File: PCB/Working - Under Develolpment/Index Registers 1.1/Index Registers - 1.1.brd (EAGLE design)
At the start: 177.8 x 114.6 mm, 83 parts, among them IC1 74LS32N, IC10 74LS32N, IC11 74LS192N, IC12 74LS192N, IC13 74LS192N, IC14 74LS192N, IC15 74LS244N, IC16 74LS244N, IC17 74LS32N, IC18 74LS192N, IC19 74LS192N, IC2 74LS32N, IC20 74LS192N, IC21 74LS192N, IC22 74LS244N, IC23 74LS244N, IC24 74LS32N, IC25 74LS192N, IC26 74LS192N, IC27 74LS192N, IC28 74LS192N, IC29 74LS244N, IC3 74LS192N, IC30 74LS244N, IC31 74LS32N, IC32 74LS139N, IC33 74LS139N, IC34 4077N, IC35 74LS245N, IC36 74LS245N, IC37 74LS245N, IC4 74LS192N, IC5 74LS192N, IC6 74LS192N, IC7 74LS244N, IC8 74LS244N, IC9 74LS32N, X1 FABC96R

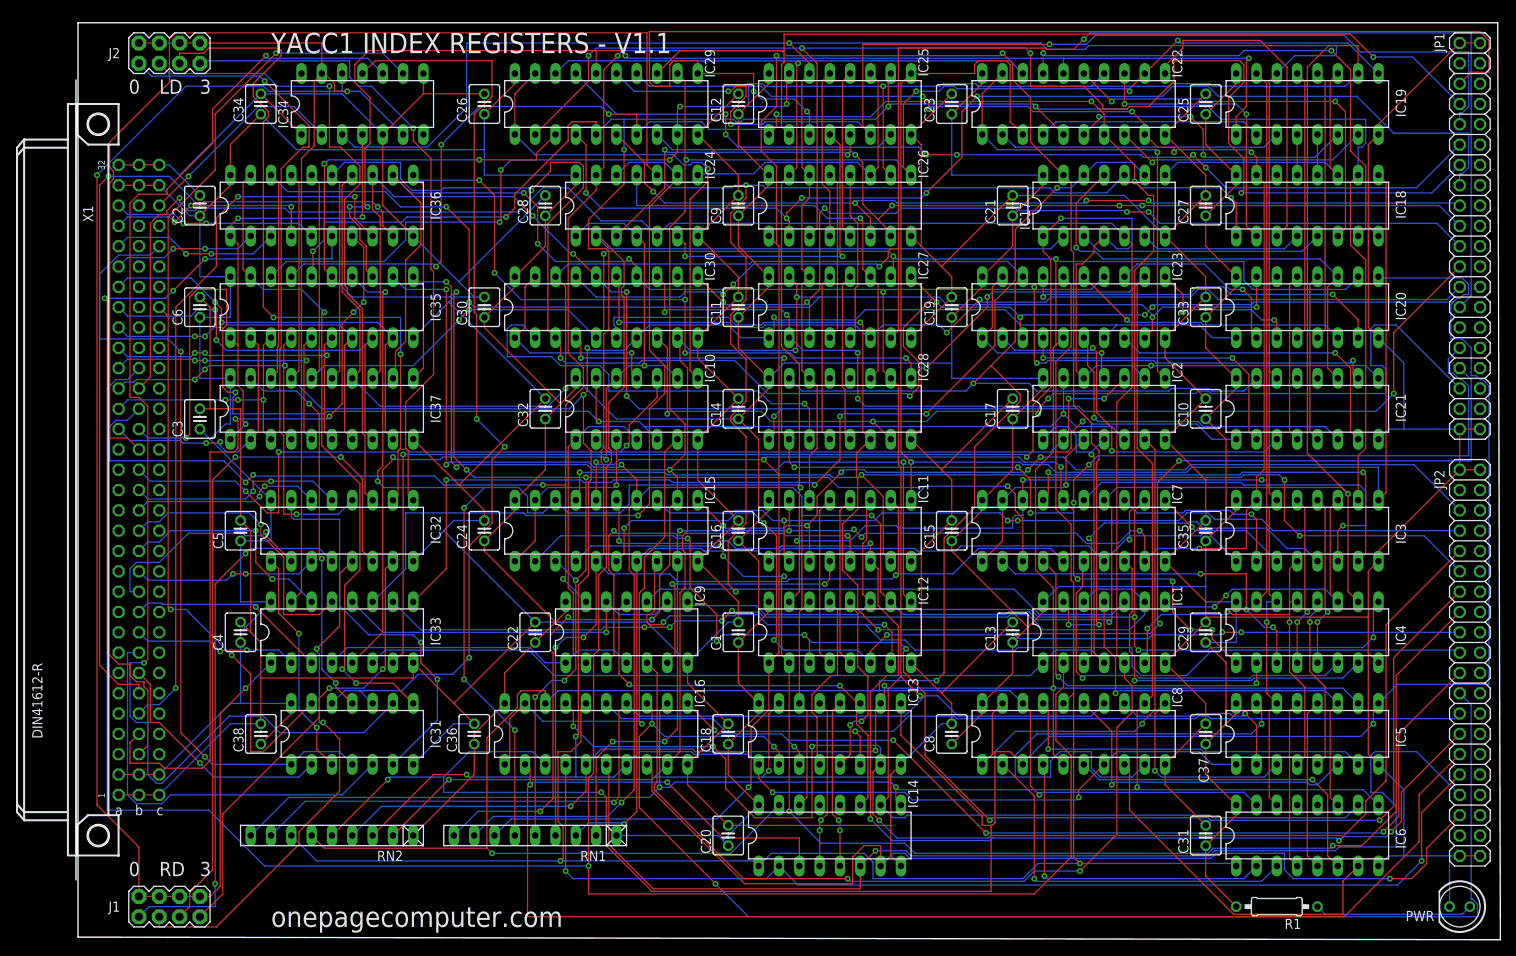
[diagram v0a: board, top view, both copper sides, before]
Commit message: Index Register Board V1.1
Modify so any data register can drive address bus
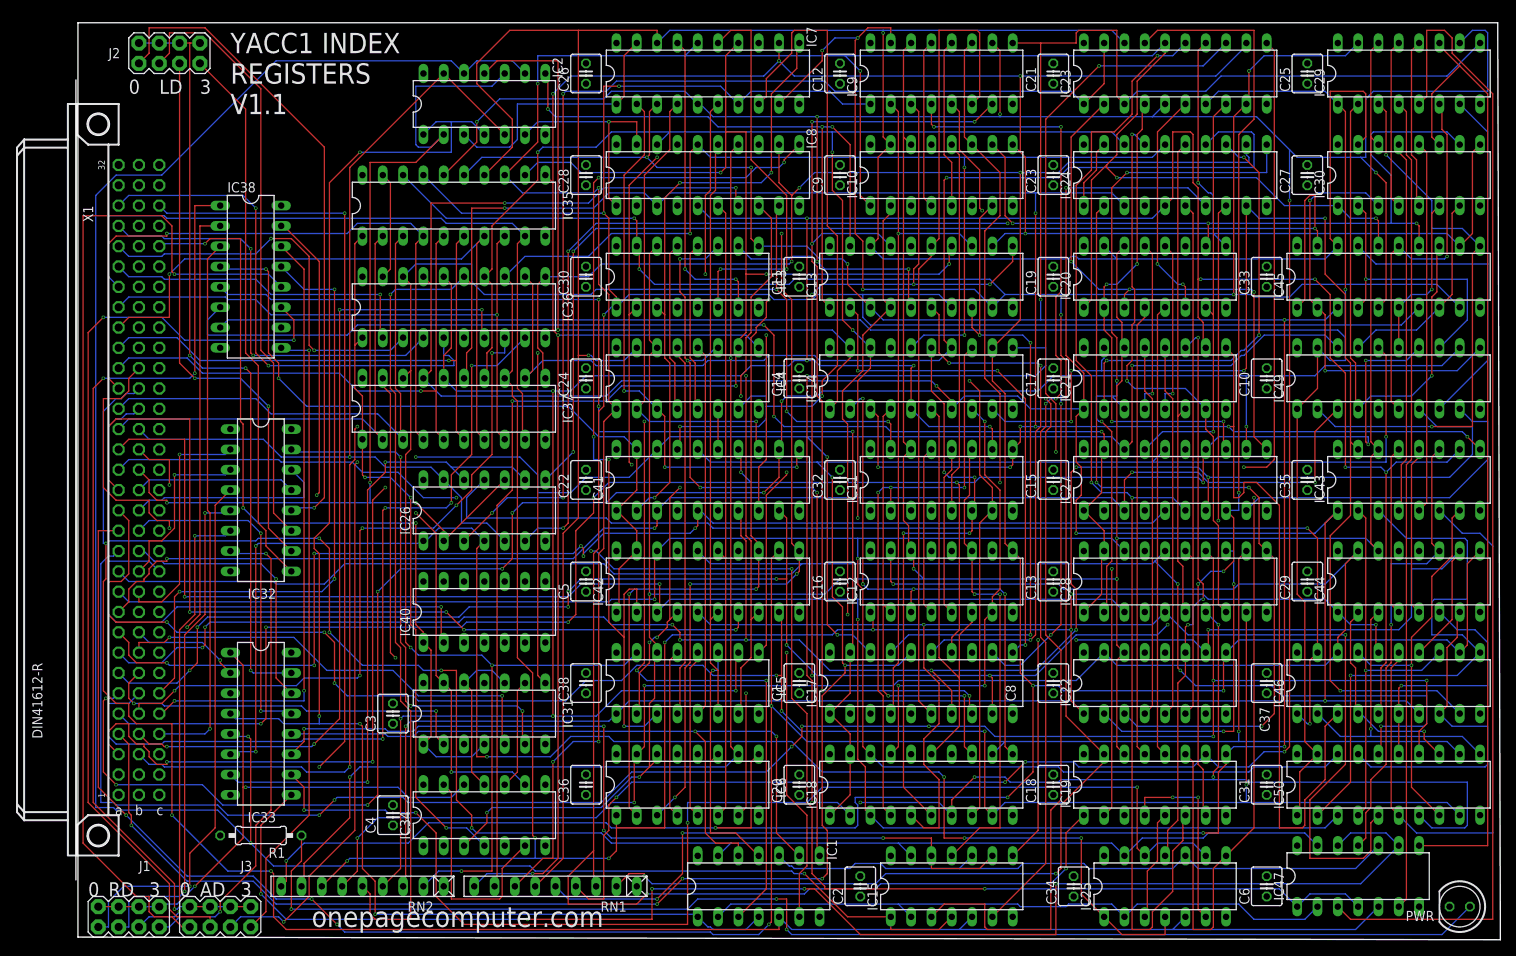
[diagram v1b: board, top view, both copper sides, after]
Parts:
- removed IC16: 74LS244N, 74xx-us:DIL20
- removed JP1, JP2: (no value), pinhead:2X20
- added IC38: 74LS139N, 74xx-us:DIL16
- added IC40, IC47: 74LS32N, 74xx-us:DIL14
- added IC41, IC42, IC45, IC46, IC49, IC50: 74LS244N, 74xx-us:DIL20
- added IC43, IC44: 74LS192N, 74xx-us:DIL16
- added J3: (no value), SparkFun-Connectors:2X4
- IC10, IC9: value 74LS32N -> 74LS192N; device 74xx-us:DIL14 -> 74xx-us:DIL16
- IC13, IC14, IC18, IC27, IC28: value 74LS192N -> 74LS244N; device 74xx-us:DIL16 -> 74xx-us:DIL20
- IC15: value 74LS244N -> 74LS32N; device 74xx-us:DIL20 -> 74xx-us:DIL14
- IC17, IC24: value 74LS32N -> 74LS244N; device 74xx-us:DIL14 -> 74xx-us:DIL20
- IC22, IC29, IC30: value 74LS244N -> 74LS192N; device 74xx-us:DIL20 -> 74xx-us:DIL16
- IC25, IC26: value 74LS192N -> 74LS32N; device 74xx-us:DIL16 -> 74xx-us:DIL14
- moved C6 151.7 mm to (148.6, 6.35)
- moved C34 141.0 mm to (124.5, 6.35)
- moved R1 127.3 mm to (22.9, 12.7)
- moved C2 118.6 mm to (97.8, 6.35)
- moved IC25 105.9 mm to (135.9, 6.35)
- moved IC30 101.7 mm to (166.4, 95.2)
- moved IC29 100.4 mm to (166.4, 108.0)
- moved IC34 90.2 mm to (50.8, 15.2)
- moved IC19 87.2 mm to (134.6, 19.1)
- moved IC18 87.0 mm to (105.4, 19.1)
- moved IC2 86.3 mm to (50.8, 104.1)
- moved IC3 83.7 mm to (76.2, 82.5)
- moved IC4 83.7 mm to (76.2, 69.8)
- moved IC8 83.5 mm to (78.7, 95.2)
- moved IC9 80.2 mm to (108.0, 108.0)
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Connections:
- net IO-ADDR0 renamed IOADDR0
- net IO-ADDR1 renamed IOADDR1
- net IO-ADDR2 renamed IOADDR2
- net IO-ADDR3 renamed IOADDR3
- removed net -ADDR-REG-LD0: X1.C4
- removed net -ADDR-REG-LD1: X1.C6
- removed net -ADDR-REG-RD0: X1.C3
- removed net -ADDR-REG-RD1: X1.C5
- removed net 1C-12: JP1.29
- removed net IA-0: IC11.3, IC15.11, JP2.5
- removed net IA-1: IC11.2, IC15.13, JP2.7
- removed net IA-10: IC13.6, IC16.15, JP2.25
- removed net IA-11: IC13.7, IC16.17, JP2.27
- removed net IA-12: IC14.3, IC16.2, JP2.29
- removed net IA-13: IC14.2, IC16.4, JP2.31
- removed net IA-14: IC14.6, IC16.6, JP2.33
- removed net IA-15: IC14.7, IC16.8, JP2.35
- removed net IA-2: IC11.6, IC15.15, JP2.9
- removed net IA-3: IC11.7, IC15.17, JP2.11
- removed net IA-4: IC12.3, IC15.2, JP2.13
- removed net IA-5: IC12.2, IC15.4, JP2.15
- removed net IA-6: IC12.6, IC15.6, JP2.17
- removed net IA-7: IC12.7, IC15.8, JP2.19
- removed net IA-8: IC13.3, IC16.11, JP2.21
- removed net IA-9: IC13.2, IC16.13, JP2.23
- removed net IB-0: JP2.6
- removed net IB-1: JP2.8
- removed net IB-10: JP2.26
- removed net IB-11: JP2.28
- removed net IB-12: JP2.30
- removed net IB-13: JP2.32
- removed net IB-14: JP2.34
- removed net IB-15: JP2.36
- removed net IB-2: JP2.10
- removed net IB-3: JP2.12
- removed net IB-4: JP2.14
- removed net IB-5: JP2.16
- removed net IB-6: JP2.18
- removed net IB-7: JP2.20
- removed net IB-8: JP2.22
- removed net IB-9: JP2.24
- removed net IC-0: IC25.3, IC29.11, JP1.5
- removed net IC-1: IC25.2, IC29.13, JP1.7
- removed net IC-10: IC27.6, IC30.15, JP1.25
- removed net IC-11: IC27.7, IC30.17, JP1.27
- removed net IC-12: IC28.3, IC30.2
- removed net IC-13: IC28.2, IC30.4, JP1.31
- removed net IC-14: IC28.6, IC30.6, JP1.33
- removed net IC-15: IC28.7, IC30.8, JP1.35
- removed net IC-2: IC25.6, IC29.15, JP1.9
- removed net IC-3: IC25.7, IC29.17, JP1.11
- removed net IC-4: IC26.3, IC29.2, JP1.13
- removed net IC-5: IC26.2, IC29.4, JP1.15
- removed net IC-6: IC26.6, IC29.6, JP1.17
- removed net IC-7: IC26.7, IC29.8, JP1.19
- removed net IC-8: IC27.3, IC30.11, JP1.21
- removed net IC-9: IC27.2, IC30.13, JP1.23
- removed net ID-0: JP1.6
- removed net ID-1: JP1.8
- removed net ID-10: JP1.26
- removed net ID-11: JP1.28
- removed net ID-12: JP1.30
- removed net ID-13: JP1.32
- removed net ID-14: JP1.34
- removed net ID-15: JP1.36
- removed net ID-2: JP1.10
- removed net ID-3: JP1.12
- removed net ID-4: JP1.14
- removed net ID-5: JP1.16
- removed net ID-6: JP1.18
- removed net ID-7: JP1.20
- removed net ID-8: JP1.22
- removed net ID-9: JP1.24
- removed net N$58 (its old number): IC18.13, IC19.4
- removed net N$59 (its old number): IC18.12, IC19.5
- removed net N$6 (its old number): IC27.13, IC28.4
- removed net N$7 (its old number): IC27.12, IC28.5
- removed net UNUSED0: X1.C12
- new net -ADDRSEL: IC38.1, J3.2, J3.4, J3.6, J3.8
- new net -ARD0: IC38.12, J3.1
- new net -R0-ADDRSEL: IC38.4, IC41.1, IC41.19, IC42.1, IC42.19
- new net -R1-ADDRSEL: IC17.1, IC17.19, IC18.1, IC18.19, IC38.5
- new net -R2-ADDRSEL: IC27.1, IC27.19, IC28.1, IC28.19, IC38.6
- new net -R3-ADDRSEL: IC38.7, IC49.1, IC49.19, IC50.1, IC50.19
- new net -VMA: IC40.2, X1.C12
- new net ADDR-REG-ID0: IC38.2, X1.C3
- new net ADDR-REG-ID1: IC38.3, X1.C4
- new net ADDR-REG-ID2: IC38.14, X1.C5
- new net ADDR-REG-ID3: IC38.13, X1.C6
- new net N$100: IC29.6, IC45.15, IC49.6
- new net N$101: IC29.7, IC45.17, IC49.8
- new net N$102: IC30.3, IC45.2, IC49.11
- new net N$103: IC30.2, IC45.4, IC49.13
- new net N$104: IC30.6, IC45.6, IC49.15
- new net N$105: IC30.7, IC45.8, IC49.17
- new net N$106: IC43.3, IC46.11, IC50.2
- new net N$107: IC43.2, IC46.13, IC50.4
- new net N$108: IC43.6, IC46.15, IC50.6
- new net N$109: IC43.7, IC46.17, IC50.8
- new net N$110: IC44.3, IC46.2, IC50.11
- new net N$111: IC44.2, IC46.4, IC50.13
- new net N$112: IC44.6, IC46.6, IC50.15
- new net N$113: IC44.7, IC46.8, IC50.17
- new net N$28: IC13.11, IC17.2, IC9.3
- new net N$29: IC13.13, IC17.4, IC9.2
- new net N$45: IC38.15, IC40.3
- new net N$51: IC38.11, J3.3
- new net N$52: IC38.10, J3.5
- new net N$53: IC38.9, J3.7
- new net N$54: IC12.3, IC14.2, IC18.11
- new net N$55: IC12.2, IC14.4, IC18.13
- new net N$56: IC12.6, IC14.6, IC18.15
- new net N$57: IC12.7, IC14.8, IC18.17
- new net N$62: IC21.13, IC22.4
- new net N$63: IC21.12, IC22.5
- new net N$67: IC23.1, IC23.19, IC26.3
- new net N$68: IC24.1, IC24.19, IC26.6
- new net N$69: IC21.11, IC22.11, IC25.11
- new net N$70: IC19.3, IC23.11, IC27.2
- new net N$71: IC19.2, IC23.13, IC27.4
- new net N$72: IC19.6, IC23.15, IC27.6
- new net N$73: IC19.7, IC23.17, IC27.8
- new net N$74: IC20.3, IC23.2, IC27.11
- new net N$75: IC20.2, IC23.4, IC27.13
- new net N$76: IC20.6, IC23.6, IC27.15
- new net N$77: IC20.7, IC23.8, IC27.17
- new net N$78: IC21.3, IC24.11, IC28.2
- new net N$79: IC21.2, IC24.13, IC28.4
- new net N$99: IC29.2, IC45.13, IC49.4
- net -BUS-EN: now also IC40.1
- net -R0-LDSEL: now also IC1.12, IC1.9; no longer IC9.12, IC9.9
- net -R0-RDSEL: now also IC1.1, IC1.4, IC2.1, IC2.4; no longer IC10.1, IC10.4, IC9.1, IC9.4
- net -R1-LDSEL: now also IC15.12, IC15.9; no longer IC24.12, IC24.9
- net -R1-RDSEL: now also IC15.1, IC15.4, IC2.12, IC2.9; no longer IC10.12, IC10.9, IC24.1, IC24.4
- net -R2-LDSEL: now also IC25.12, IC25.9; no longer IC1.12, IC1.9
- net -R2-RDSEL: now also IC25.1, IC25.4, IC26.1, IC26.4; no longer IC1.1, IC1.4, IC2.1, IC2.4
- net -R3-LDSEL: now also IC47.12, IC47.9; no longer IC17.12, IC17.9
- net -R3-RDSEL: now also IC26.12, IC26.9, IC47.1, IC47.4; no longer IC17.1, IC17.4, IC2.12, IC2.9
- net -REG-DN: now also IC15.5, IC25.5, IC47.5; no longer IC17.5, IC24.5, IC9.5
- net -REG-LD-HI: now also IC15.13, IC25.13, IC47.13; no longer IC17.13, IC24.13, IC9.13
- net -REG-LD-LO: now also IC15.10, IC25.10, IC47.10; no longer IC17.10, IC24.10, IC9.10
- net -REG-RD-HI: now also IC26.13, IC26.5; no longer IC10.13, IC10.5
- net -REG-RD-LO: now also IC26.10, IC26.2; no longer IC10.10, IC10.2
- net -REG-UP: now also IC15.2, IC25.2, IC47.2; no longer IC17.2, IC24.2, IC9.2
- net ADATA0: now also IC13.9, IC19.15, IC23.9, IC29.15, IC45.9, IC9.15; no longer IC11.15, IC15.9, IC18.15, IC22.9, IC25.15, IC29.9
- net ADATA1: now also IC13.7, IC19.1, IC23.7, IC29.1, IC45.7, IC9.1; no longer IC11.1, IC15.7, IC18.1, IC22.7, IC25.1, IC29.7
- net ADATA10: now also IC11.10, IC14.5, IC21.10, IC24.5, IC43.10, IC46.5; no longer IC13.10, IC16.5, IC20.10, IC23.5, IC27.10, IC30.5
- net ADATA11: now also IC11.9, IC14.3, IC21.9, IC24.3, IC43.9, IC46.3; no longer IC13.9, IC16.3, IC20.9, IC23.3, IC27.9, IC30.3
- net ADATA12: now also IC12.15, IC14.18, IC22.15, IC24.18, IC44.15, IC46.18; no longer IC14.15, IC16.18, IC21.15, IC23.18, IC28.15, IC30.18
- net ADATA13: now also IC12.1, IC14.16, IC22.1, IC24.16, IC44.1, IC46.16; no longer IC14.1, IC16.16, IC21.1, IC23.16, IC28.1, IC30.16
- net ADATA14: now also IC12.10, IC14.14, IC22.10, IC24.14, IC44.10, IC46.14; no longer IC14.10, IC16.14, IC21.10, IC23.14, IC28.10, IC30.14
- net ADATA15: now also IC12.9, IC14.12, IC22.9, IC24.12, IC44.9, IC46.12; no longer IC14.9, IC16.12, IC21.9, IC23.12, IC28.9, IC30.12
- net ADATA2: now also IC13.5, IC19.10, IC23.5, IC29.10, IC45.5, IC9.10; no longer IC11.10, IC15.5, IC18.10, IC22.5, IC25.10, IC29.5
- net ADATA3: now also IC13.3, IC19.9, IC23.3, IC29.9, IC45.3, IC9.9; no longer IC11.9, IC15.3, IC18.9, IC22.3, IC25.9, IC29.3
- net ADATA4: now also IC10.15, IC13.18, IC20.15, IC23.18, IC30.15, IC45.18; no longer IC12.15, IC15.18, IC19.15, IC22.18, IC26.15, IC29.18
- net ADATA5: now also IC10.1, IC13.16, IC20.1, IC23.16, IC30.1, IC45.16; no longer IC12.1, IC15.16, IC19.1, IC22.16, IC26.1, IC29.16
- net ADATA6: now also IC10.10, IC13.14, IC20.10, IC23.14, IC30.10, IC45.14; no longer IC12.10, IC15.14, IC19.10, IC22.14, IC26.10, IC29.14
- net ADATA7: now also IC10.9, IC13.12, IC20.9, IC23.12, IC30.9, IC45.12; no longer IC12.9, IC15.12, IC19.9, IC22.12, IC26.9, IC29.12
- net ADATA8: now also IC11.15, IC14.9, IC21.15, IC24.9, IC43.15, IC46.9; no longer IC13.15, IC16.9, IC20.15, IC23.9, IC27.15, IC30.9
- net ADATA9: now also IC11.1, IC14.7, IC21.1, IC24.7, IC43.1, IC46.7; no longer IC13.1, IC16.7, IC20.1, IC23.7, IC27.1, IC30.7
- net ADDR0: now also IC17.18, IC27.18, IC41.18, IC49.18
- net ADDR1: now also IC17.16, IC27.16, IC41.16, IC49.16
- net ADDR10: now also IC18.14, IC28.14, IC42.14, IC50.14
- net ADDR11: now also IC18.12, IC28.12, IC42.12, IC50.12
- net ADDR12: now also IC18.9, IC28.9, IC42.9, IC50.9
- net ADDR13: now also IC18.7, IC28.7, IC42.7, IC50.7
- net ADDR14: now also IC18.5, IC28.5, IC42.5, IC50.5
- net ADDR15: now also IC18.3, IC28.3, IC42.3, IC50.3
- net ADDR2: now also IC17.14, IC27.14, IC41.14, IC49.14
- net ADDR3: now also IC17.12, IC27.12, IC41.12, IC49.12
- net ADDR4: now also IC17.9, IC27.9, IC41.9, IC49.9
- net ADDR5: now also IC17.7, IC27.7, IC41.7, IC49.7
- net ADDR6: now also IC17.5, IC27.5, IC41.5, IC49.5
- net ADDR7: now also IC17.3, IC27.3, IC41.3, IC49.3
- net ADDR8: now also IC18.18, IC28.18, IC42.18, IC50.18
- net ADDR9: now also IC18.16, IC28.16, IC42.16, IC50.16
- net GND: now also IC10.8, IC13.10, IC14.10, IC15.7, IC17.10, IC18.10, IC22.8, IC24.10, IC25.7, IC26.7, IC27.10, IC28.10, IC29.8, IC30.8, IC38.8, IC40.7, IC41.10, IC42.10, IC43.8, IC44.8, IC45.10, IC46.10, IC47.7, IC49.10, IC50.10, IC9.8; no longer IC10.7, IC13.8, IC14.8, IC15.10, IC16.10, IC17.7, IC18.8, IC22.10, IC24.7, IC25.8, IC26.8, IC27.8, IC28.8, IC29.10, IC30.10, IC9.7, JP1.1, JP1.2, JP1.39, JP1.40, JP2.1, JP2.2, JP2.39, JP2.40
- net N$115: now also IC41.2
- net N$116: now also IC41.4
- net N$117: now also IC41.6
- net N$118: now also IC41.8
- net N$119: now also IC41.11
- net N$120: now also IC41.13
- net N$121: now also IC41.15
- net N$122: now also IC41.17
- net N$123: now also IC42.2
- net N$124: now also IC42.4
- net N$125: now also IC42.6
- net N$126: now also IC42.8
- net N$127: now also IC42.11
- net N$128: now also IC42.13
- net N$129: now also IC42.15
- net N$130: now also IC42.17
- net N$2: now also IC10.4, IC9.13; no longer IC25.13, IC26.4
- net N$23: now also IC15.6, IC9.4; no longer IC24.6, IC25.4
- net N$25: now also IC13.1, IC13.19, IC2.8; no longer IC10.8, IC29.1, IC29.19
- net N$26: now also IC14.1, IC14.19, IC2.11; no longer IC10.11, IC30.1, IC30.19
- net N$27: now also IC11.11, IC12.11, IC15.11; no longer IC24.11, IC27.11, IC28.11
- net N$3: now also IC10.5, IC9.12; no longer IC25.12, IC26.5
- net N$30: now also IC13.15, IC17.6, IC9.6; no longer IC12.13, IC13.4
- net N$31: now also IC13.17, IC17.8, IC9.7; no longer IC12.12, IC13.5
- net N$32: now also IC10.3, IC13.2, IC17.11; no longer IC13.13, IC14.4
- net N$33: now also IC10.2, IC13.4, IC17.13; no longer IC13.12, IC14.5
- net N$34: now also IC10.6, IC13.6, IC17.15; no longer IC11.11, IC12.11, IC9.8
- net N$35: now also IC10.7, IC13.8, IC17.17; no longer IC11.5, IC9.3
- net N$36: now also IC11.3, IC14.11, IC18.2; no longer IC11.4, IC9.6
- net N$38: now also IC11.2, IC14.13, IC18.4; no longer IC10.3, IC15.1, IC15.19
- net N$39: now also IC11.6, IC14.15, IC18.6; no longer IC10.6, IC16.1, IC16.19
- net N$4: now also IC10.13, IC11.4; no longer IC26.13, IC27.4
- net N$40: now also IC11.7, IC14.17, IC18.8; no longer IC13.11, IC14.11, IC9.11
- net N$5: now also IC10.12, IC11.5; no longer IC26.12, IC27.5
- net N$64: now also IC20.11, IC25.8; no longer IC17.8, IC18.11
- net N$65: now also IC19.5, IC25.3; no longer IC17.3, IC18.5
- net N$66: now also IC19.4, IC25.6; no longer IC17.6, IC18.4
- net N$8: now also IC10.11, IC15.8, IC9.11; no longer IC24.8, IC25.11, IC26.11
- net N$80: now also IC21.6, IC24.15, IC28.6; no longer IC18.3, IC22.11
- net N$81: now also IC21.7, IC24.17, IC28.8; no longer IC18.2, IC22.13
- net N$82: now also IC22.3, IC24.2, IC28.11; no longer IC18.6, IC22.15
- net N$83: now also IC22.2, IC24.4, IC28.13; no longer IC18.7, IC22.17
- net N$84: now also IC22.6, IC24.6, IC28.15; no longer IC2.8, IC22.1, IC22.19
- net N$85: now also IC22.7, IC24.8, IC28.17; no longer IC2.11, IC23.1, IC23.19
- net N$86: now also IC29.13, IC30.4; no longer IC17.11, IC20.11, IC21.11
- net N$87: now also IC29.12, IC30.5; no longer IC19.3, IC22.2
- net N$88: now also IC30.13, IC43.4; no longer IC19.2, IC22.4
- net N$89: now also IC30.12, IC43.5; no longer IC19.6, IC22.6
- net N$9: now also IC15.3, IC9.5; no longer IC24.3, IC25.5
- net N$90: now also IC43.13, IC44.4; no longer IC19.7, IC22.8
- net N$91: now also IC43.12, IC44.5; no longer IC20.3, IC23.11
- net N$92: now also IC29.11, IC30.11, IC47.8; no longer IC20.2, IC23.13
- net N$93: now also IC29.5, IC47.3; no longer IC20.6, IC23.15
- net N$94: now also IC29.4, IC47.6; no longer IC20.7, IC23.17
- net N$95: now also IC26.8, IC45.1, IC45.19; no longer IC21.3, IC23.2
- net N$96: now also IC26.11, IC46.1, IC46.19; no longer IC21.2, IC23.4
- net N$97: now also IC43.11, IC44.11, IC47.11; no longer IC21.6, IC23.6
- net N$98: now also IC29.3, IC45.11, IC49.2; no longer IC21.7, IC23.8
- net RESET: now also IC10.14, IC22.14, IC29.14, IC30.14, IC43.14, IC44.14, IC9.14; no longer IC13.14, IC14.14, IC18.14, IC25.14, IC26.14, IC27.14, IC28.14
- net VCC: now also IC10.16, IC13.20, IC14.20, IC15.14, IC17.20, IC18.20, IC22.16, IC24.20, IC25.14, IC26.14, IC27.20, IC28.20, IC29.16, IC30.16, IC38.16, IC40.14, IC41.20, IC42.20, IC43.16, IC44.16, IC45.20, IC46.20, IC47.14, IC49.20, IC50.20, IC9.16; no longer IC10.14, IC13.16, IC14.16, IC15.20, IC16.20, IC17.14, IC18.16, IC22.20, IC24.14, IC25.16, IC26.16, IC27.16, IC28.16, IC29.20, IC30.20, IC9.14
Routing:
- net GND: track 970.6 -> 0.00 mm
- net VCC: track 788.7 -> 0.00 mm
- net ADDR11: track 0.00 -> 288.8 mm, vias 0 -> 6
- net ADDR3: track 0.00 -> 281.4 mm, vias 0 -> 11
- net ADDR10: track 0.00 -> 277.2 mm, vias 0 -> 8
- net ADDR1: track 0.00 -> 271.6 mm, vias 0 -> 7
- net ADDR13: track 0.00 -> 259.1 mm, vias 0 -> 8
- net ADDR0: track 0.00 -> 246.5 mm, vias 0 -> 7
- net ADDR9: track 0.00 -> 246.4 mm, vias 0 -> 3
- net ADDR12: track 0.00 -> 242.9 mm, vias 0 -> 7
- net ADDR5: track 0.00 -> 239.8 mm, vias 0 -> 9
- net ADDR15: track 0.00 -> 239.2 mm, vias 0 -> 3
- net ADDR14: track 0.00 -> 238.8 mm, vias 0 -> 3
- net ADDR2: track 0.00 -> 233.8 mm, vias 0 -> 9
- net ADDR4: track 0.00 -> 227.2 mm, vias 0 -> 8
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- added copper zone on layer 15, net GND
- added copper zone on layer 2, net VCC
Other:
- board text added: "AD"
- board text added: "YACC1 INDEX REGISTERS V1.1"
- board text removed: "YACC1 INDEX REGISTERS - V1.1"
